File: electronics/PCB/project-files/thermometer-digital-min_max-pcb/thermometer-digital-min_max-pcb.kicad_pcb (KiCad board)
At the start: 4 copper layers, 100 x 75 mm, 33 parts, among them J0 sensor_connection, J1 battery_connection, Q0 PN2222A, Q1 PN2222A, Q2 PN2222A, Q3 PN2222A, U0 ATmega328P-U

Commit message: Testing signing
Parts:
- moved R12 8.61 mm to (168.2, 106.9)
- moved J0 8.22 mm to (175.8, 110.2)
- moved B0 4.96 mm to (186.7, 61.5)
- moved R0 4.63 mm to (141.5, 58.1)
- moved B1 4.55 mm to (110.7, 61.5)
- moved Q0 4.46 mm to (172.8, 92.3)
- moved Q1 4.38 mm to (159.8, 92.3)
- moved Q2 4.32 mm to (146.8, 92.3)
- moved Q3 4.28 mm to (133.8, 92.3)
- moved R11 4.17 mm to (175.3, 88.8)
- moved R10 4.09 mm to (162.3, 88.8)
- moved R9 4.02 mm to (149.3, 88.8)
- moved J1 3.99 mm to (133.3, 110.1)
- moved R8 3.98 mm to (136.3, 88.8)
- moved D0 3.89 mm to (166.4, 85.1)
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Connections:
- U0 pad 10: unconnected-(U0-Pad10) -> GND
- U0 pad 19: unconnected-(U0-Pad19) -> GND
- U0 pad 20: unconnected-(U0-Pad20) -> GND
- U0 pad 21: unconnected-(U0-Pad21) -> GND
- U0 pad 27: unconnected-(U0-Pad27) -> GND
- U0 pad 28: unconnected-(U0-Pad28) -> GND
- U0 pad 9: unconnected-(U0-Pad9) -> GND
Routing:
- net Net-(B2-Pad1): track 92.9 -> 6.50 mm
- net /SS_C: track 84.3 -> 9.12 mm
- net /SS_D: track 92.3 -> 21.7 mm
- net /SS_G: track 81.0 -> 13.6 mm
- net Net-(B1-Pad1): track 64.6 -> 6.50 mm
- net /SS_DP: track 78.6 -> 21.1 mm
- net /SS_F: track 73.4 -> 21.3 mm, vias 0 -> 1
- net Net-(R4-Pad1): track 7.18 -> 53.6 mm
- net Net-(R3-Pad1): track 6.66 -> 48.4 mm
- net /SS_A: track 49.5 -> 8.19 mm
- net Net-(R11-Pad1): track 75.0 -> 114.9 mm
- net Net-(R2-Pad1): track 6.09 -> 40.9 mm
- net /SS_E: track 89.9 -> 55.8 mm
- net /SS_B: track 48.4 -> 14.6 mm
- net Net-(R5-Pad1): track 6.66 -> 35.9 mm
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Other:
- copper layers 4 -> 2

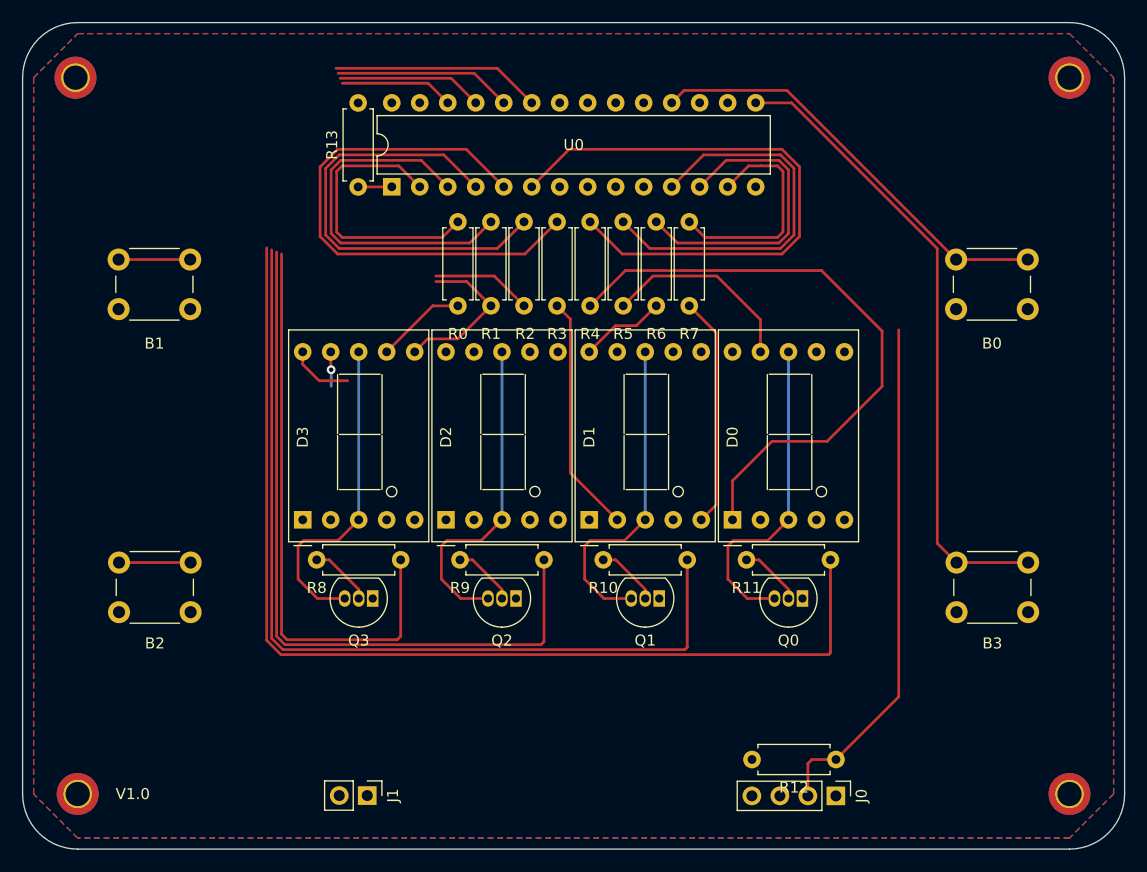
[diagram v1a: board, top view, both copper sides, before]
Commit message: Completed the relayout of the PCB
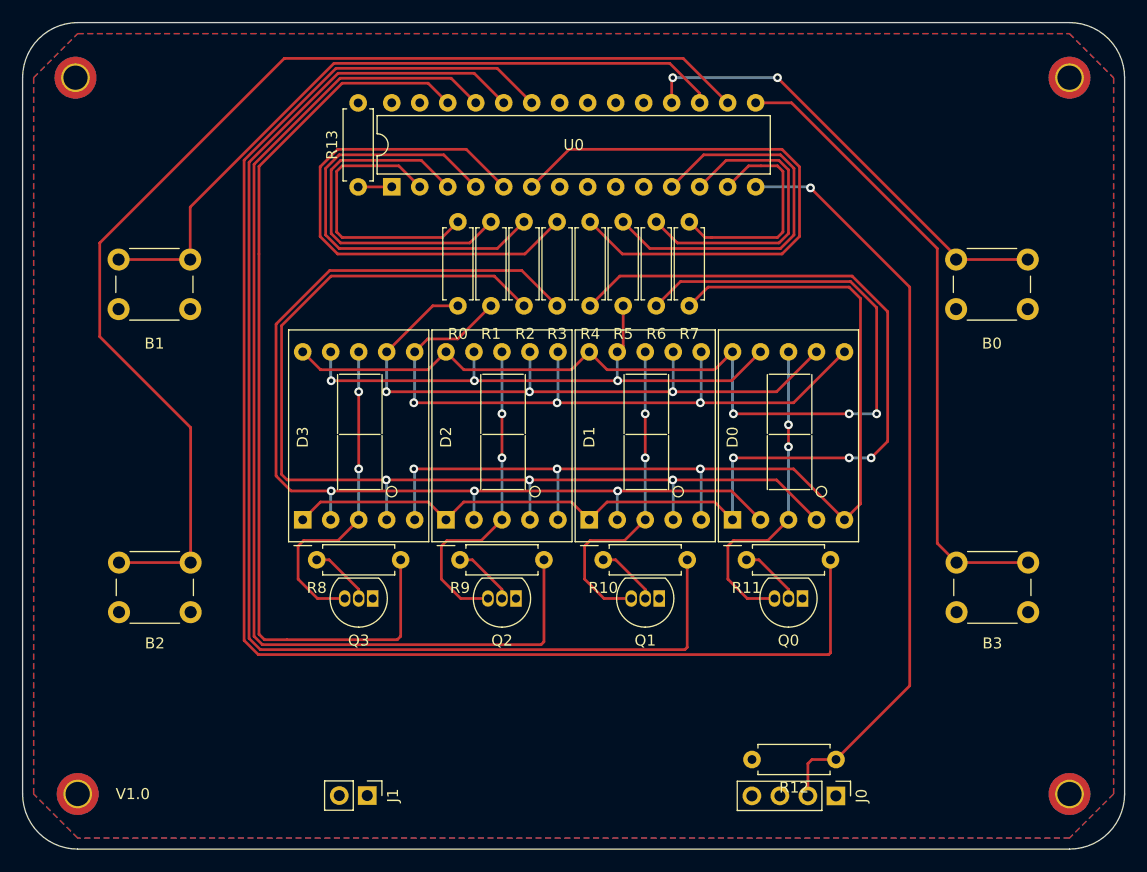
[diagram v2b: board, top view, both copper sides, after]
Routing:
- net Net-(B2-Pad1): track 6.50 -> 104.5 mm
- net /SS_C: track 9.12 -> 99.6 mm, vias 0 -> 3
- net /SS_G: track 13.6 -> 93.2 mm, vias 0 -> 3
- net /SS_D: track 21.7 -> 96.1 mm, vias 0 -> 3
- net /SS_DP: track 21.1 -> 92.3 mm, vias 0 -> 3
- net Net-(B1-Pad1): track 6.50 -> 64.9 mm
- net /SS_A: track 8.19 -> 59.6 mm, vias 0 -> 3
- net /SS_B: track 14.6 -> 63.6 mm, vias 0 -> 3
- net /SS_E: track 55.8 -> 104.5 mm, vias 0 -> 3
- net /SS_F: track 21.3 -> 52.4 mm, vias 1 -> 3
- net Net-(J0-Pad2): track 47.0 -> 69.0 mm, vias 0 -> 1
- net Net-(R11-Pad1): track 114.9 -> 136.7 mm
- net Net-(R10-Pad1): track 97.6 -> 119.0 mm
- net Net-(R9-Pad1): track 80.2 -> 101.3 mm
- net Net-(R8-Pad1): track 62.9 -> 83.6 mm
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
